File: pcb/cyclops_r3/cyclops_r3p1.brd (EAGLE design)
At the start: 69.8 x 53.3 mm, 53 parts, among them Q1 SUM11006, Q2 N-MOSFETTO-262, U1 MCP4921, U2 317-N, U3 ADR03, U4 OP1177, U5 LM324N

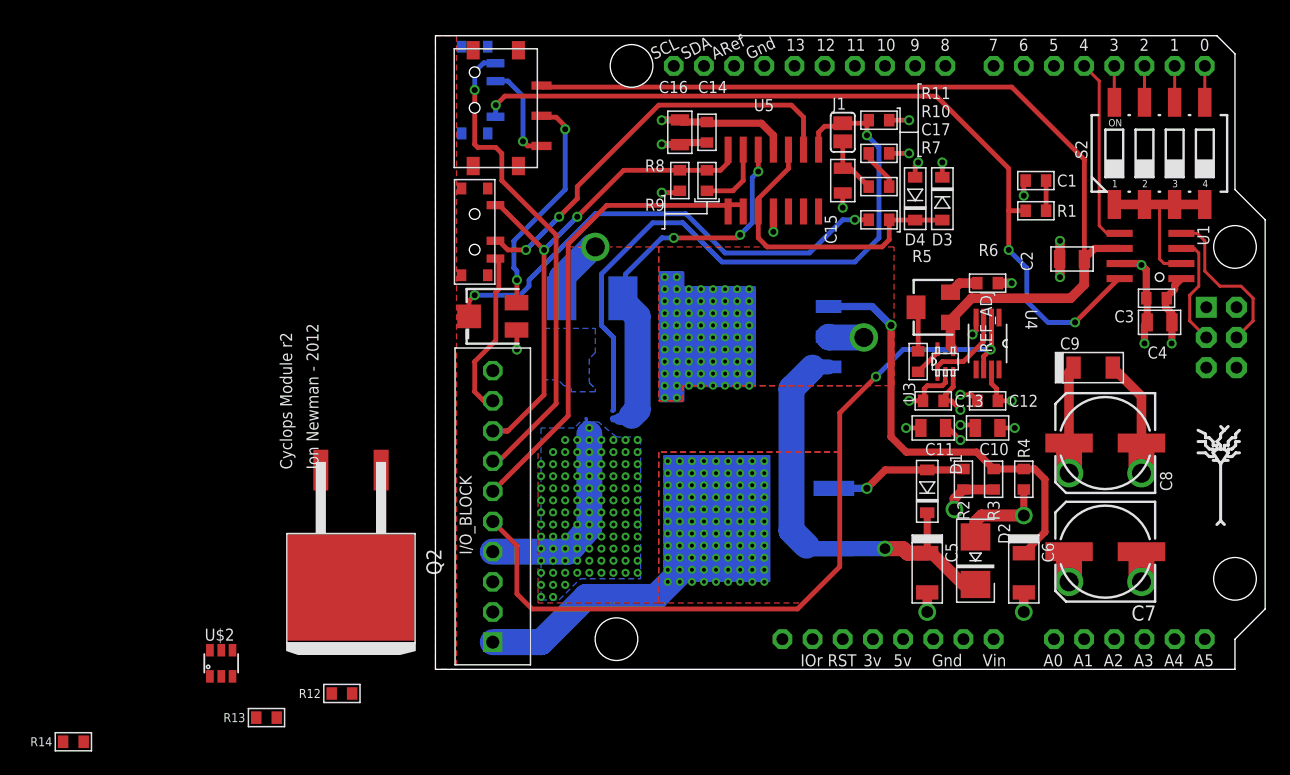
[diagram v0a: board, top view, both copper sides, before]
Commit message: Silkscreen added to revision 3.1
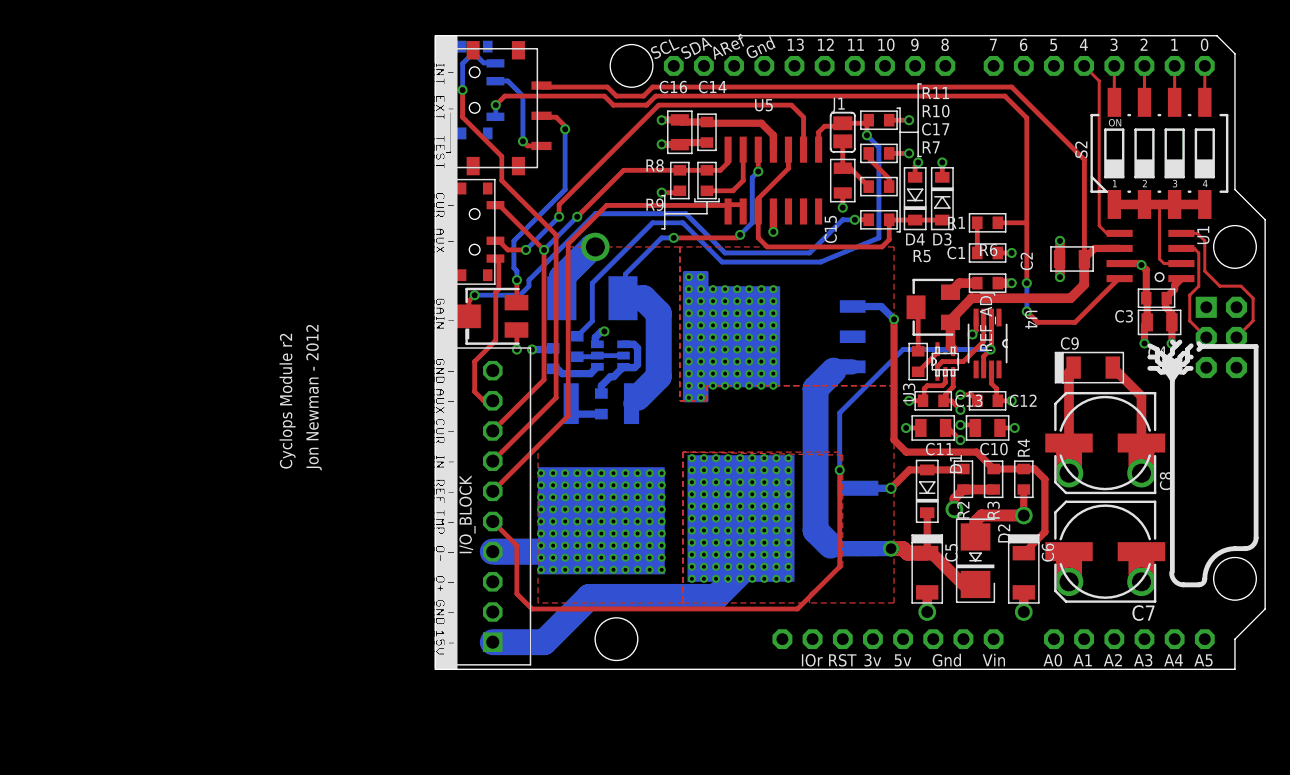
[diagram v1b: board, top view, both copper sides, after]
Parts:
- removed U$2: (no value), cyclops:SOT23-6
- added U6: (no value), cyclops:SOT23-6
- Q2: value N-MOSFETTO-262 -> IRF510
- R12: value 0 -> 0R
- R13: value 12 -> 12R, 1W
- R14: value 1 -> 1R, 1W
- RSENSE: value 0.1 -> 0.1, 1W
- moved R14 52.8 mm to (12.7, 22.4), flipped to the bottom, turned to 270 degrees
- moved R13 38.7 mm to (8.64, 26.2), flipped to the bottom, turned to 270 degrees
- moved R12 35.3 mm to (10.7, 27.2), flipped to the bottom, turned to 90 degrees
- moved Q2 21.8 mm to (12.7, 17.0), flipped to the bottom
- moved C1 7.33 mm to (45.2, 35.1), turned to 0 degrees
- moved R1 4.19 mm to (45.2, 37.6), turned to 0 degrees
- moved Q1 2.03 mm to (29.0, 12.7)
- moved U2 2.03 mm to (26.7, 28.0)
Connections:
- removed net AGND: U$2.3
- net +12V: no longer Q2.D
- net GND: now also U6.3
- net LED-: now also Q2.D
- net N$10: now also U6.4, U6.6; no longer U$2.4, U$2.6
- net N$12: now also U6.1; no longer U$2.1
- net N$9: now also U6.2, U6.5; no longer U$2.2, U$2.5
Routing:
- net LED-: track 18.4 -> 10.4 mm, vias 111 -> 99
- net N$10: track 0.00 -> 7.21 mm
- net N$3: track 55.8 -> 49.5 mm
- net DACA: track 70.3 -> 75.9 mm
- net +15V: track 24.2 -> 28.8 mm
- net N$12: track 0.00 -> 4.13 mm
- net N$9: track 0.00 -> 3.94 mm
- net N$13: track 0.00 -> 3.63 mm
- net N$18: track 11.6 -> 9.55 mm
- net VI: track 44.4 -> 42.3 mm
- net +15V_RECT: track 36.8 -> 34.9 mm
- net N$72: track 36.7 -> 35.1 mm
- net GND: track 65.7 -> 67.2 mm, vias 25 -> 26
- net +12V: track 46.0 -> 44.9 mm
- net VINPUT: track 41.1 -> 42.2 mm
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- removed copper zone on layer 16, net LED-
- removed copper zone on layer 16, net N$5
- removed copper zone on layer 1, net N$8
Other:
- board text removed: "15V"
- board text removed: "AUX"
- board text removed: "CUR"
- board text removed: "CUR AUX"
- board text removed: "GAIN"
- board text removed: "GND"
- board text removed: "IN"
- board text removed: "INT EXT"
- board text removed: "O+"
- board text removed: "O-"
- board text removed: "REF"
- board text removed: "TEST"
- board text removed: "TMP"

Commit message: Some updates to the library and board. Also, update the design rules so that vias are not exposed solder.
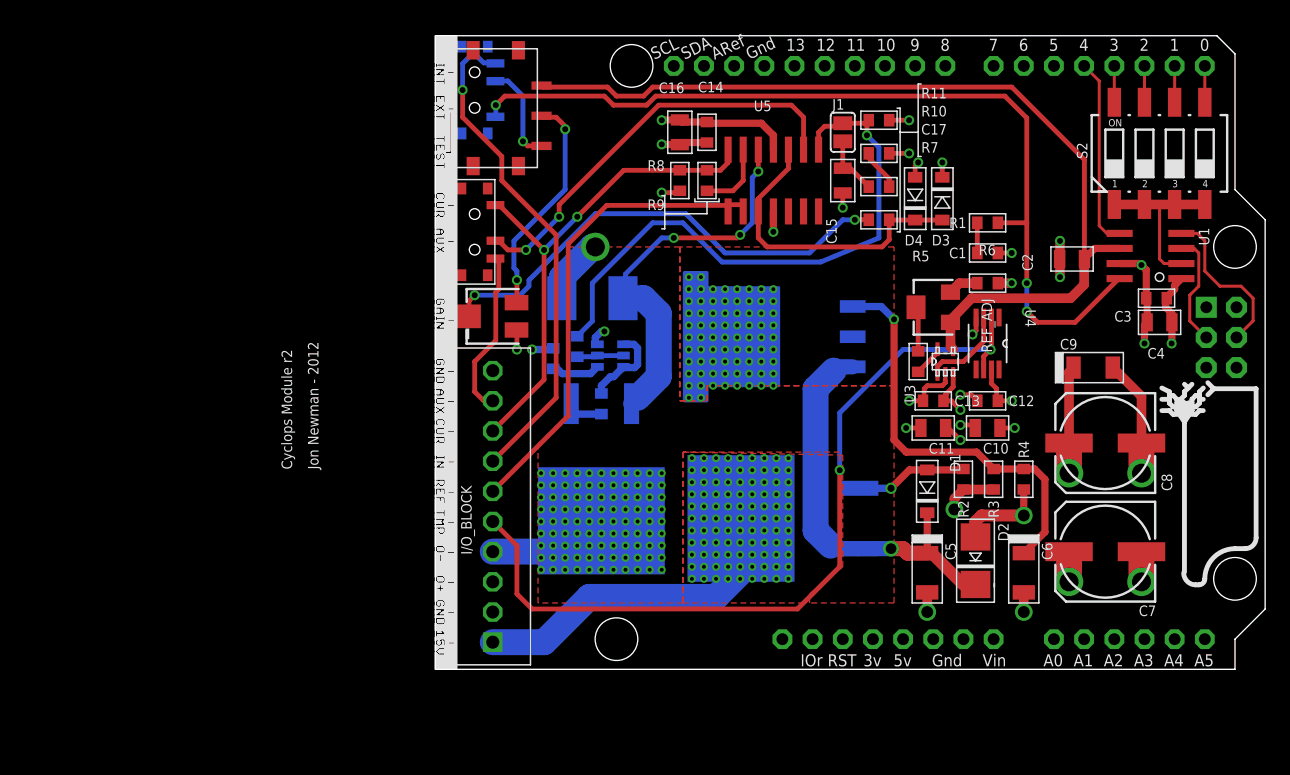
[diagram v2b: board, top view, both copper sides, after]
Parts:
- D2: device cyclops:SMA-DO214AC@1 -> cyclops:SMA-DO214AC
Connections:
- removed net GND$1: U$1.GND$1
- removed net GND$2: U$1.GND$2
- net GND: now also U$1.GND$1, U$1.GND$2

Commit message: Reimplemented NMOS bias network after merge issues.
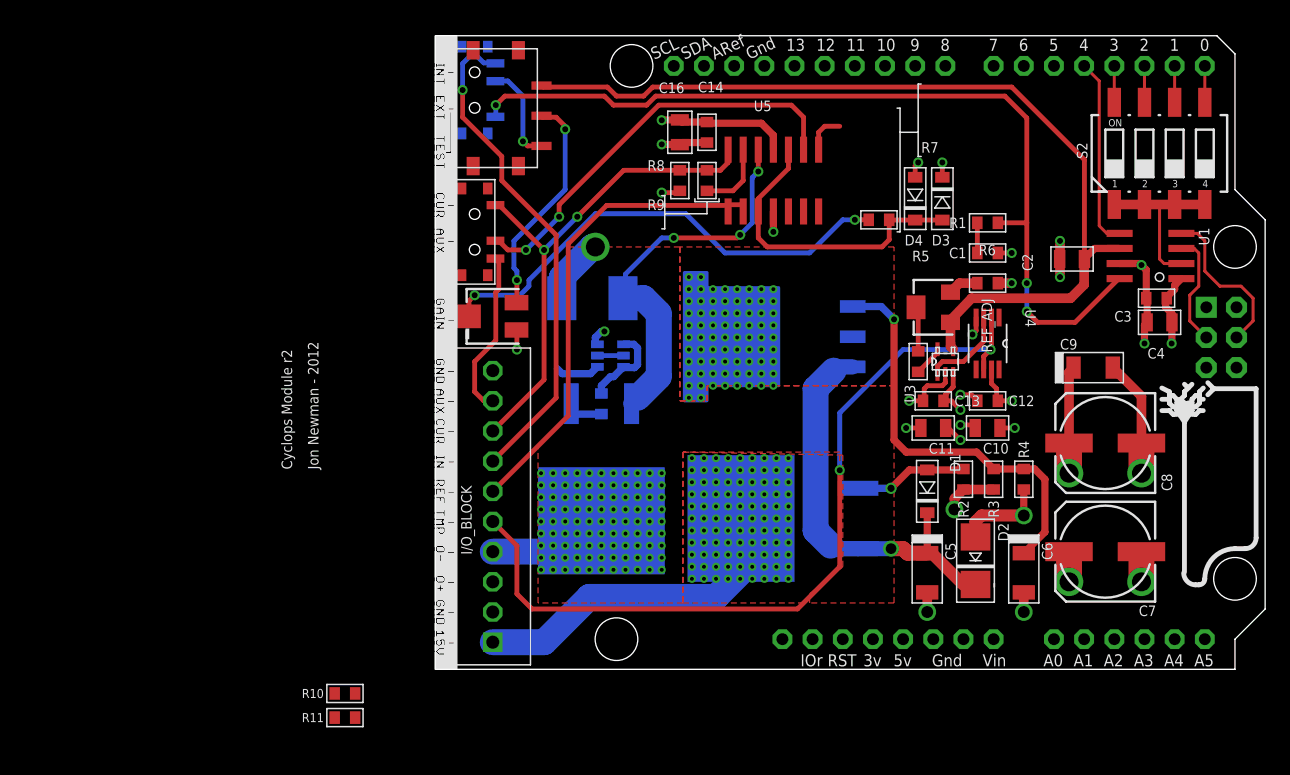
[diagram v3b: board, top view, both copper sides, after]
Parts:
- removed C15: 1uF, cyclops:0805
- removed C17: 0.1uF, cyclops:0603
- removed J1: (no value), jumper:SJ
- removed R12: 0R, cyclops:0603
- removed R13: 12R, 1W, cyclops:0603
- R10: value 120 -> 1.1k
- R11: value 220k -> 560
- R14: value 1R, 1W -> 560
- moved R11 67.5 mm to (-8.89, -4.06), turned to 0 degrees
- moved R10 63.9 mm to (-8.89, -2.03), turned to 0 degrees
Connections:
- removed net N$11: C15.1, C17.1, J1.1
- removed net N$4: C17.2, R10.2
- removed net N$9: R12.1, U6.2, U6.5
- new net AGND: R11.1
- net +12V: now also R10.2; no longer R13.1
- net GND: no longer C15.2, R10.1, R11.1
- net N$12: no longer R13.2
- net N$13: now also R10.1, R11.2
- net N$3: now also U6.2, U6.5; no longer J1.2, R11.2, R12.2
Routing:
- net N$3: track 49.5 -> 5.80 mm, vias 1 -> 0
- net N$11: track 5.09 -> 0.00 mm
- net GND: track 67.2 -> 62.6 mm, vias 26 -> 23
- net N$9: track 3.94 -> 0.00 mm
- net N$4: track 3.51 -> 0.00 mm
- net +12V: track 44.9 -> 43.0 mm, vias 86 -> 85

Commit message: Added NMOS bias network to the layout.
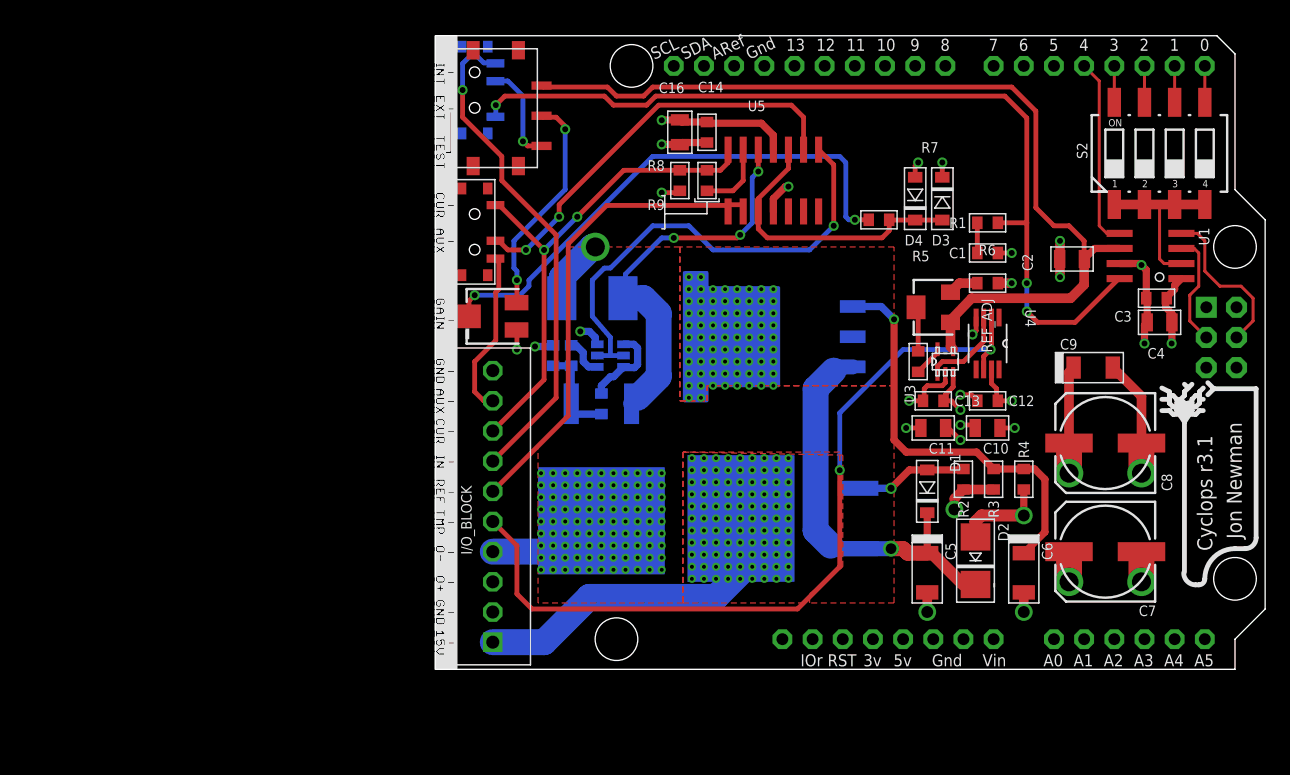
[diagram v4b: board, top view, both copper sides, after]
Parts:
- moved R11 35.2 mm to (8.64, 26.4), flipped to the bottom, turned to 270 degrees
- moved R10 34.2 mm to (10.2, 26.4), flipped to the bottom, turned to 90 degrees
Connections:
- removed net AGND: R11.1
- removed net N$12: U6.1
- net +12V: now also U6.1
- net GND: now also R11.1
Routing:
- net N$3: track 5.80 -> 40.1 mm, vias 0 -> 1
- net N$13: track 3.63 -> 8.34 mm
- net N$7: track 40.8 -> 45.2 mm
- net N$12: track 3.78 -> 0.00 mm
- net +12V: track 43.0 -> 46.4 mm
- net GND: track 62.6 -> 65.8 mm, vias 23 -> 24
- net _VREF: track 26.2 -> 24.7 mm
- net REFA: track 77.8 -> 78.8 mm
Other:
- board text added: "Cyclops r3.1"
- board text added: "Jon Newman"
- board text removed: "Cyclops Module r2"
- board text removed: "Jon Newman - 2012"

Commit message: Not too sure what I did here, to be honest.
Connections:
- removed net 5V: U$1.+5V
- net +5V: now also U$1.+5V
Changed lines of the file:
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@@
 <wire x1="39.37" y1="30.3" x2="39.19" y2="30.48" width="0.4064" layer="1"/>
-</signal>
-<signal name="5V">
-<contactref element="U$1" pad="+5V"/>
 </signal>
 <signal name="3V">
@@
 <wire x1="60.198" y1="30.48" x2="60.7314" y2="29.9466" width="0.6096" layer="1"/>
 <wire x1="60.7314" y1="29.9466" x2="60.7314" y2="29.21" width="0.6096" layer="1"/>
+<contactref element="U$1" pad="+5V"/>
+<wire x1="61.528" y1="32.893" x2="66.167" y2="30.48" width="0" layer="19" extent="1-1"/>
 </signal>
 <signal name="SCLK">

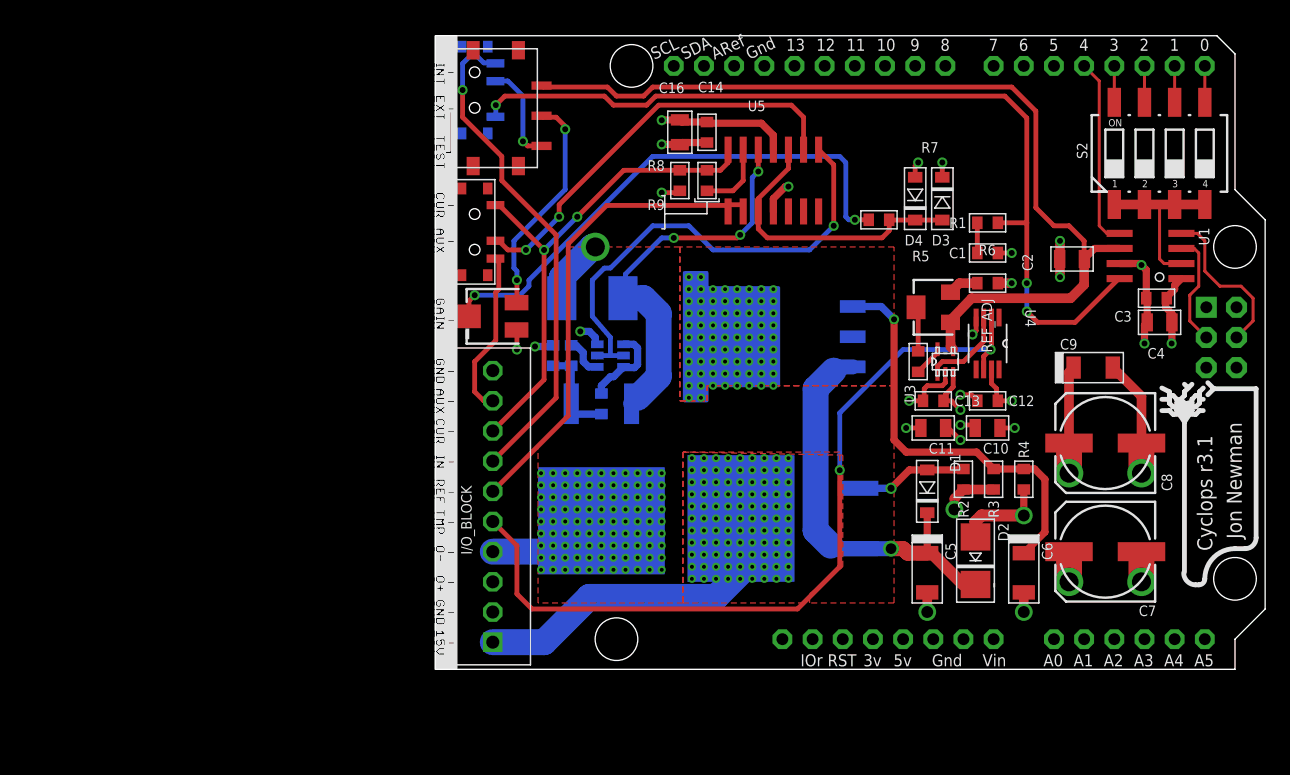
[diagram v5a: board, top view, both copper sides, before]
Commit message: The board is pretty much finished. I need to verify a few components and add a bottom silkscreen with detailed board info before fabrication, though. Also, there are some ERC issues that are not really problems, but should be fixed on the schematic for perfection's sake.
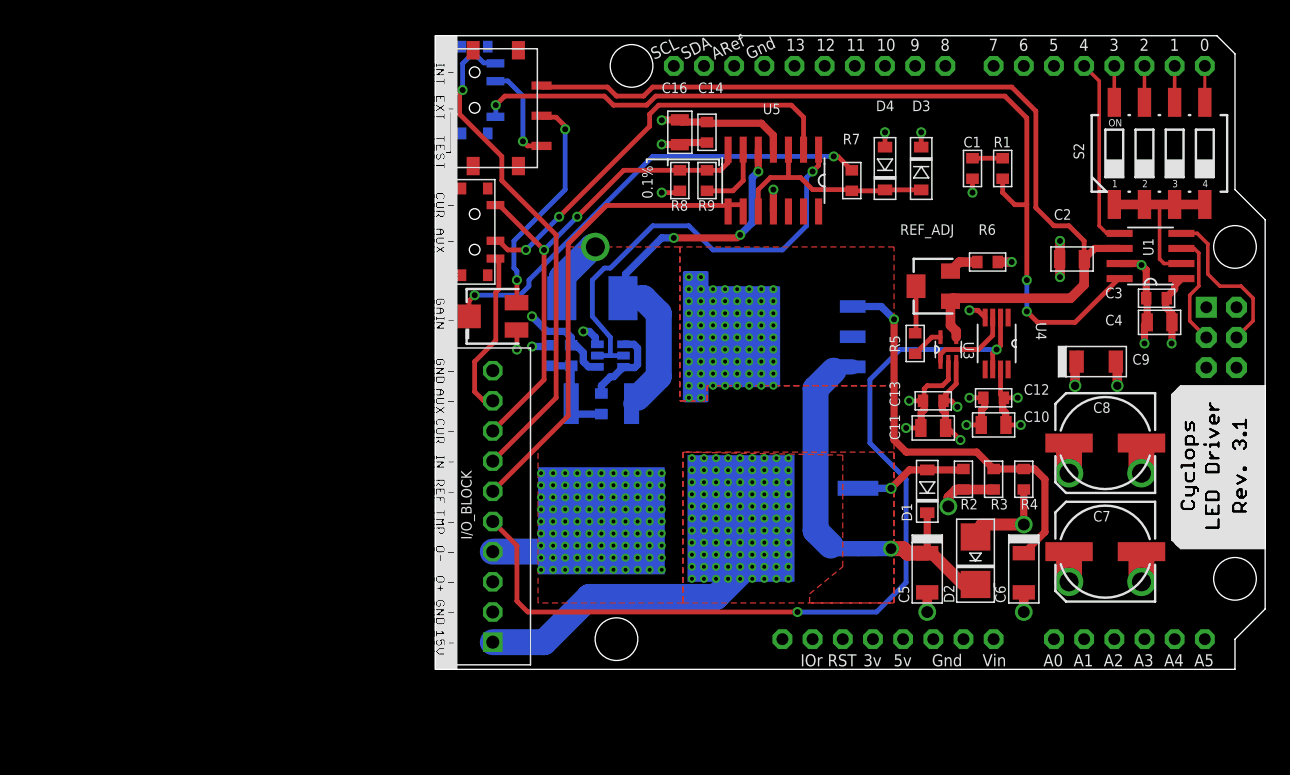
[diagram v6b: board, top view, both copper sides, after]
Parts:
- C12, C13, C14, C3: value 0.1uF -> .1uF
- D1: value MMSZ5240B -> MMSZ
- D2: value S1B-13-F -> S1B
- R8: value 1k 0.1% -> 1k
- R9: value 9k 0.1% -> 9k
- RSENSE: value 0.1, 1W -> 0.1,1W
- U6: value (none) -> ZXTD45
- moved C1 7.22 mm to (43.9, 42.2), turned to 270 degrees
- moved R1 4.75 mm to (46.5, 42.2), turned to 270 degrees
- moved R7 4.02 mm to (33.8, 41.1), turned to 270 degrees
- moved D4 3.59 mm to (36.6, 42.2)
- moved D3 3.10 mm to (39.6, 42.2)
- moved REF_ADJ 1.78 mm to (40.6, 32.3)
- moved R6 1.78 mm to (45.2, 34.3)
- moved R5 1.55 mm to (39.1, 27.4)
- moved U3 1.05 mm to (41.9, 26.9)
- moved U4 0.76 mm to (46.0, 27.4)
- moved C9 0.57 mm to (54.4, 25.9)
- moved C10 0.57 mm to (45.7, 20.6)
- moved C12 0.57 mm to (45.7, 22.9)
- moved R11 0.25 mm to (8.38, 26.4)
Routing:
- net VTEMP: track 68.6 -> 76.4 mm
- net +12V: track 46.4 -> 52.8 mm, vias 85 -> 87
- net _VREF: track 24.7 -> 18.8 mm
- net N$7: track 45.2 -> 39.3 mm
- net N$3: track 40.1 -> 37.7 mm
- net DACA: track 75.9 -> 77.0 mm
- net GND: vias 24 -> 25
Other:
- board text added: "0.1%"
- board text removed: "Cyclops r3.1"
- board text removed: "Jon Newman"
